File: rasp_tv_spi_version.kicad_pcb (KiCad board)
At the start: 2 copper layers, 118.3 x 53.5 mm, 12 parts, among them J1 Raspberry_Pi_2_3, J6 PAM8302-input, J7 PAM8302-output, J8 SPEAKER, J9 5V_USB, SW1 SW_Push_DPDT, U1 TFT_320x240

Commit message: make pcb routing
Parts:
- removed J9 (x2): 5V_USB, Connector_Wire:SolderWirePad_1x01_SMD_1.5x3mm
- removed U1: TFT_320x240, Display:TFT-320x240
- added J3: Conn_01x09, Connector_PinHeader_2.54mm:PinHeader_1x09_P2.54mm_Vertical_SMD_Pin1Left, F.Cu at (166.6, 91.1)
- added J4: AUODIO_IN, Connector_PinHeader_2.54mm:PinHeader_1x05_P2.54mm_Vertical_SMD_Pin1Left, F.Cu at (184.0, 77.5)
- added J5: SPEAKER, Connector_PinHeader_2.54mm:PinHeader_1x02_P2.54mm_Horizontal, B.Cu at (181.6, 87.6)
- added REF**: PinHeader_1x04_P2.54mm_Vertical, Connector_PinHeader_2.54mm:PinHeader_1x04_P2.54mm_Vertical, F.Cu at (85.6, 80.9)
- J1: footprint Connector_PinHeader_2.54mm:PinHeader_2x20_P2.54mm_Vertical -> Connector_PinSocket_2.54mm:PinSocket_2x20_P2.54mm_Vertical
- J6: value PAM8302-input -> AUDIO_OUT; footprint Connector_PinHeader_2.54mm:PinHeader_1x05_P2.54mm_Vertical -> Connector_PinSocket_2.54mm:PinSocket_1x02_P2.54mm_Vertical_SMD_Pin1Left; moved to F.Cu
- J7: value PAM8302-output -> AUDIO_OUT; footprint Connector_PinHeader_2.54mm:PinHeader_1x02_P2.54mm_Vertical -> Connector_PinSocket_2.54mm:PinSocket_1x02_P2.54mm_Vertical_SMD_Pin1Left; moved to F.Cu
- J8: value SPEAKER -> Conn_01x02_Pin; footprint Connector_Hirose:Hirose_DF13C_CL535-0402-2-51_1x02-1MP_P1.25mm_Vertical -> Connector_PinHeader_2.54mm:PinHeader_1x02_P2.54mm_Horizontal; moved to B.Cu
- SW1: footprint Button_Switch_THT:SW_Push_2P2T_Toggle_CK_PVA2OAH5xxxxxxV2 -> Button_Switch_THT:SW_DPDT_XLX
- moved J8 37.1 mm to (181.7, 103.5), turned to 0 degrees
- moved J6 33.8 mm to (186.9, 94.9), turned to -90 degrees
- moved J7 33.8 mm to (180.9, 94.9), turned to -90 degrees
- moved R2 30.9 mm to (145.4, 64.5)
- moved J1 30.0 mm to (91.5, 64.0)
- moved C1 29.0 mm to (145.3, 67.7)
- moved R1 28.4 mm to (145.3, 70.9)
- moved RV1 26.9 mm to (180.3, 63.5)
- moved SW1 21.8 mm to (187.9, 111.4), turned to 180 degrees
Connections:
- J1 pad 16: unconnected-(J1-GPIO23-Pad16) -> BACKLIGHT_23_GPIO
- J6 pad 1: Net-(J6-Pin_1) -> unconnected-(J6-Pin_1-Pad1)
- J6 pad 2: GND -> Net-(J5-Pin_1)
- J7 pad 1: Net-(J7-Pin_1) -> Net-(J5-Pin_2)
- J7 pad 2: Net-(J7-Pin_2) -> unconnected-(J7-Pin_2-Pad2)
- J8 pad 1: Net-(J7-Pin_1) -> Net-(J8-Pin_1)
- J8 pad 2: Net-(J7-Pin_2) -> Net-(J8-Pin_2)
- RV1 pad : GND -> (no net)
- RV1 pad 2: Net-(J6-Pin_1) -> AUDIO_IN
- SW1 pad 3: Net-(J9-Pin_2) -> Net-(J8-Pin_1)
- SW1 pad 4: unconnected-(SW1-A-Pad4) -> Net-(J8-Pin_2)
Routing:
- net +5V: track 31.5 -> 183.3 mm
- net BACKLIGHT_23_GPIO: track 0.00 -> 82.5 mm
- net +3.3V: track 38.2 -> 106.5 mm
- net CS_8_GPIO: track 46.2 -> 96.3 mm
- net GND: track 45.9 -> 0.00 mm
- net RESET_25_GPIO: track 48.3 -> 86.8 mm
- net DC_24_GPIO: track 46.6 -> 83.3 mm
- net Net-(J6-Pin_1): track 19.6 -> 0.00 mm
- net MOSI_0_10_GPIO: track 57.9 -> 77.3 mm
- net Net-(J7-Pin_2): track 18.6 -> 0.00 mm
- net AUDIO_IN: track 0.00 -> 16.6 mm
- net Net-(J7-Pin_1): track 14.7 -> 0.00 mm
- net Net-(J9-Pin_2): track 11.4 -> 0.00 mm
- net SCK_0_11_GPIO: track 57.8 -> 68.6 mm
- net Net-(J5-Pin_1): track 0.00 -> 10.6 mm
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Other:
- board size 118.3 x 53.5 mm -> 120 x 60 mm

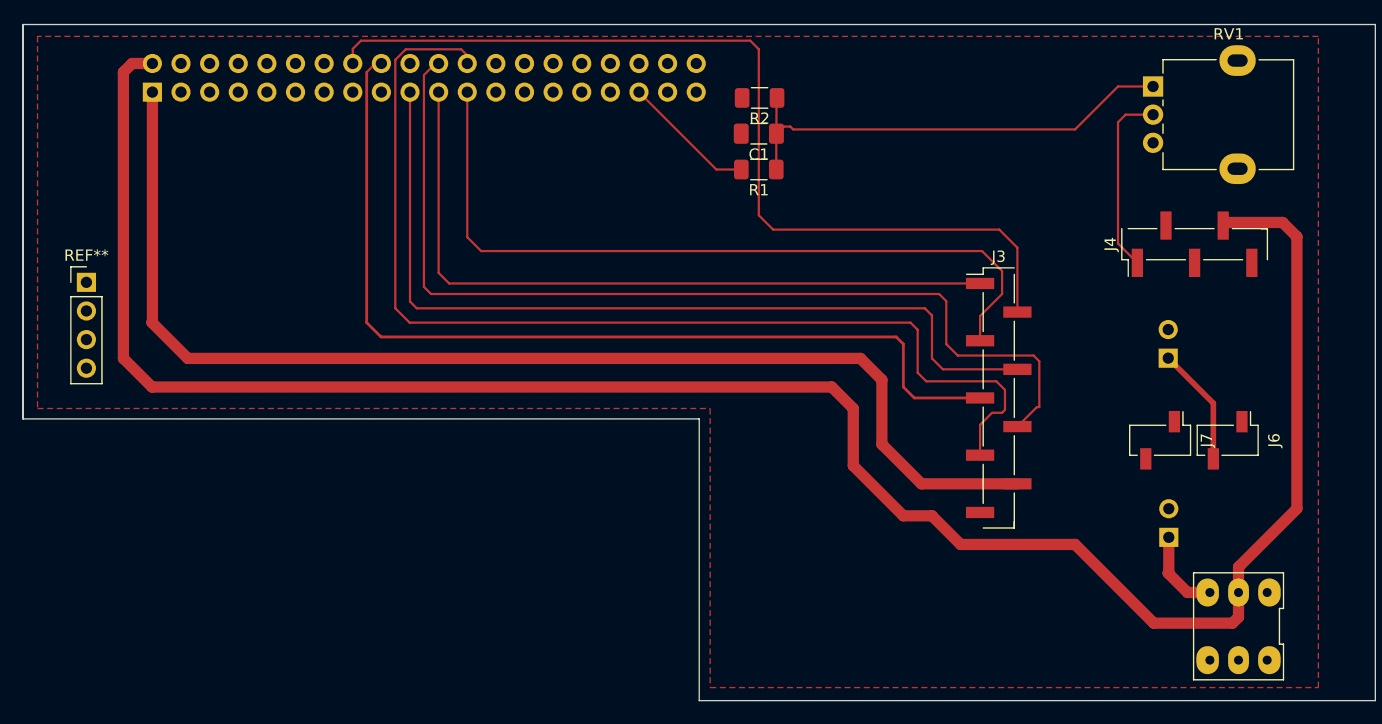
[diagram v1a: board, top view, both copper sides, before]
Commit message: finish board with 2.8 spi
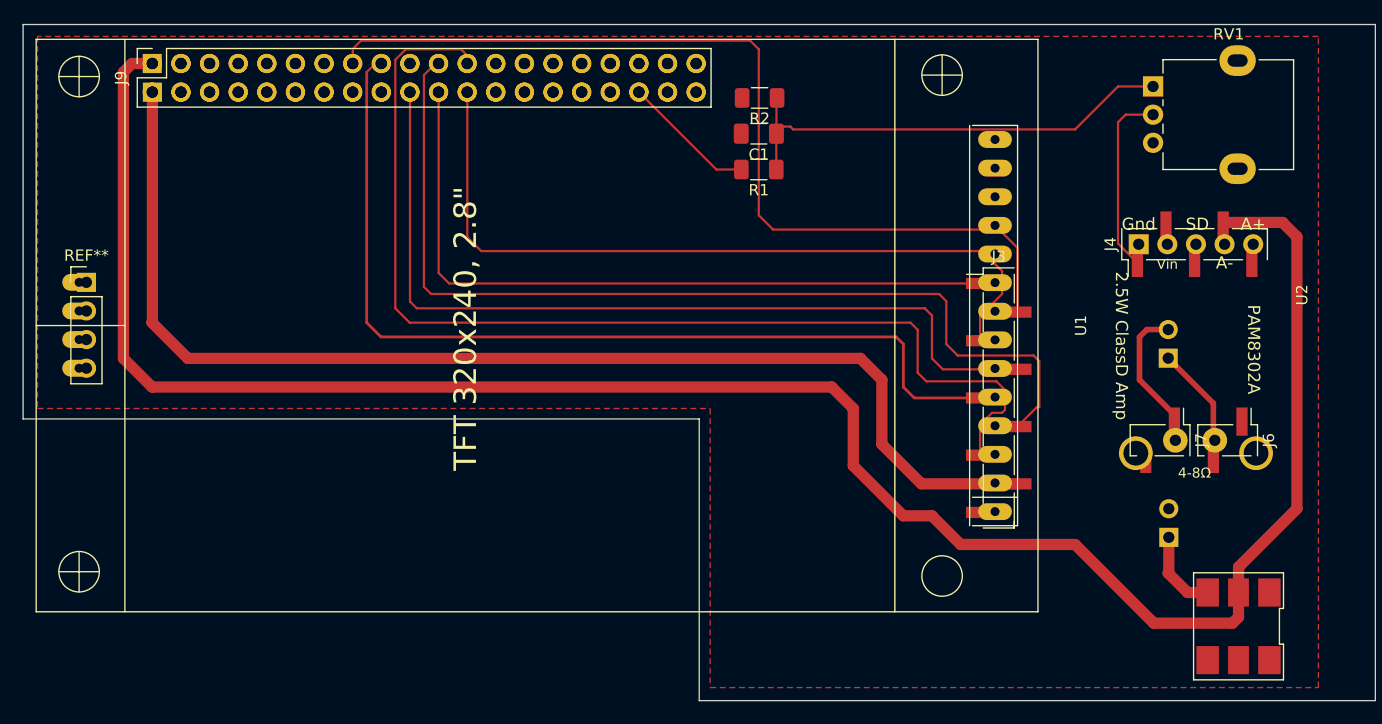
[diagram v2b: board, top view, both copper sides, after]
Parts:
- added J9: Raspberry_Pi_2_3, Connector_PinSocket_2.54mm:PinSocket_2x20_P2.54mm_Vertical, F.Cu at (91.5, 61.5)
- added U1: TFT_320x240, Display:TFT-320x240, F.Cu at (85.0, 106.6)
- added U2: PAM8302AAD, Module:PAM, F.Cu at (179.0, 77.5)
- J6, J7: footprint Connector_PinSocket_2.54mm:PinSocket_1x02_P2.54mm_Vertical_SMD_Pin1Left -> Connector_PinHeader_2.54mm:PinHeader_1x02_P2.54mm_Vertical_SMD_Pin1Left
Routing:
- net Net-(J5-Pin_2): track 0.00 -> 11.6 mm

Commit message: release 2.8
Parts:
- moved C1 62.2 mm to (91.0, 37.3)
- moved J3 62.2 mm to (112.3, 60.7)
- moved J4 62.2 mm to (129.7, 47.1)
- moved J5 62.2 mm to (127.4, 57.2)
- moved R1 62.2 mm to (91.0, 40.4)
- moved R2 62.2 mm to (91.1, 34.1)
- moved RV1 62.2 mm to (126.0, 33.1)
- moved U1 62.2 mm to (30.7, 76.1)
- moved U2 62.2 mm to (124.8, 47.1)
- moved J1 62.2 mm to (37.2, 33.6)
- moved J6 62.2 mm to (132.6, 64.5)
- moved J9 62.2 mm to (37.2, 31.0)
- moved REF** 62.2 mm to (31.4, 50.5)
- moved SW1 62.2 mm to (133.6, 81.0)
- moved J7 62.2 mm to (126.7, 64.5)
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
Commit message: ready for factory
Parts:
- removed the J4 at (129.7, 47.1)
- removed the J6 at (132.6, 64.5)
- removed the J7 at (126.7, 64.5)
- removed the J8 at (127.4, 73.1)
- removed REF**: PinHeader_1x04_P2.54mm_Vertical, Connector_PinHeader_2.54mm:PinHeader_1x04_P2.54mm_Vertical
- removed U2: PAM8302AAD, Module:PAM
- added 0.1u: C_Rect_L4.0mm_W2.5mm_P2.50mm, Capacitor_THT:C_Rect_L4.0mm_W2.5mm_P2.50mm, B.Cu at (247.6, 65.6)
- added 0.1u: C_Rect_L4.0mm_W2.5mm_P2.50mm, Capacitor_THT:C_Rect_L4.0mm_W2.5mm_P2.50mm, B.Cu at (224.6, 92.8)
- added 0.1u: C_Rect_L4.0mm_W2.5mm_P2.50mm, Capacitor_THT:C_Rect_L4.0mm_W2.5mm_P2.50mm, B.Cu at (249.5, 134.7)
- added 0.1u: C_Rect_L4.0mm_W2.5mm_P2.50mm, Capacitor_THT:C_Rect_L4.0mm_W2.5mm_P2.50mm, B.Cu at (97.5, 24.4)
- added 0.1u: C_Rect_L4.0mm_W2.5mm_P2.50mm, Capacitor_THT:C_Rect_L4.0mm_W2.5mm_P2.50mm, B.Cu at (122.4, 65.6)
- added 0.1u: C_Rect_L4.0mm_W2.5mm_P2.50mm, Capacitor_THT:C_Rect_L4.0mm_W2.5mm_P2.50mm, B.Cu at (222.6, 23.9)
- added 0.1uF: 0.1uF, Capacitor_SMD:C_1206_3216Metric_Pad1.33x1.80mm_HandSolder, F.Cu at (96.4, 26.3)
- added 0.1uF: 0.1uF, Capacitor_SMD:C_1206_3216Metric_Pad1.33x1.80mm_HandSolder, F.Cu at (125.2, 65.7)
- added 0.1uF: 0.1uF, Capacitor_SMD:C_1206_3216Metric_Pad1.33x1.80mm_HandSolder, F.Cu at (250.4, 65.7)
- added 0.1uF: 0.1uF, Capacitor_SMD:C_1206_3216Metric_Pad1.33x1.80mm_HandSolder, F.Cu at (252.3, 134.8)
- added 0R: R_1206_3216Metric, Resistor_SMD:R_1206_3216Metric, F.Cu at (186.5, 25.6)
- added 0R: R_1206_3216Metric, Resistor_SMD:R_1206_3216Metric, F.Cu at (188.5, 94.6)
- added 0R: R_1206_3216Metric, Resistor_SMD:R_1206_3216Metric, F.Cu at (237.0, 59.0)
- added 0R: R_1206_3216Metric, Resistor_SMD:R_1206_3216Metric, F.Cu at (239.3, 127.9)
- added 0R: , Resistor_SMD:R_1206_3216Metric, F.Cu at (61.5, 25.6)
- added 0R: , Resistor_SMD:R_1206_3216Metric, F.Cu at (111.6, 58.9)
- added 100R: R_Axial_DIN0204_L3.6mm_D1.6mm_P5.08mm_Horizontal, Resistor_THT:R_Axial_DIN0204_L3.6mm_D1.6mm_P5.08mm_Horizontal, B.Cu at (223.8, 30.9)
- added 100R: R_Axial_DIN0204_L3.6mm_D1.6mm_P5.08mm_Horizontal, Resistor_THT:R_Axial_DIN0204_L3.6mm_D1.6mm_P5.08mm_Horizontal, B.Cu at (225.8, 99.8)
- added 100R: R_Axial_DIN0204_L3.6mm_D1.6mm_P5.08mm_Horizontal, Resistor_THT:R_Axial_DIN0204_L3.6mm_D1.6mm_P5.08mm_Horizontal, B.Cu at (98.8, 31.0)
- added 100uF: CP_Radial_D5.0mm_P2.50mm, Capacitor_THT:CP_Radial_D5.0mm_P2.50mm, B.Cu at (249.9, 61.8)
- added 100uF: CP_Radial_D5.0mm_P2.50mm, Capacitor_THT:CP_Radial_D5.0mm_P2.50mm, B.Cu at (251.8, 130.9)
- added 100uF: CP_Radial_D5.0mm_P2.50mm, Capacitor_THT:CP_Radial_D5.0mm_P2.50mm, B.Cu at (124.7, 61.8)
- added 1K: 1K, Potentiometer_THT:Potentiometer_Alpha_RD901F-40-00D_Single_Vertical, F.Cu at (124.3, 22.1)
- added 220R: , Resistor_SMD:R_1206_3216Metric_Pad1.30x1.75mm_HandSolder, F.Cu at (96.2, 21.6)
- added 220R: 220R, Resistor_THT:R_Axial_DIN0204_L3.6mm_D1.6mm_P5.08mm_Horizontal, B.Cu at (98.8, 19.8)
- added 220R: 220R, Resistor_THT:R_Axial_DIN0204_L3.6mm_D1.6mm_P5.08mm_Horizontal, B.Cu at (225.8, 88.6)
- added 220R: 220R, Resistor_THT:R_Axial_DIN0204_L3.6mm_D1.6mm_P5.08mm_Horizontal, B.Cu at (223.8, 19.7)
- added ?: , , F.Cu at (251.8, 130.9)
- added ?: , , F.Cu at (247.6, 65.6)
- added ?: , , F.Cu at (252.3, 136.4)
- added ?: , , F.Cu at (247.6, 68.1)
- added ?: , , F.Cu at (224.6, 92.8)
- added C1: 0.1uF, Capacitor_SMD:C_1206_3216Metric_Pad1.33x1.80mm_HandSolder, F.Cu at (223.4, 95.3)
- added HOLD: PinHeader_1x02_P2.54mm_Vertical_SMD_Pin1Right, Connector_PinHeader_2.54mm:PinHeader_1x02_P2.54mm_Vertical_SMD_Pin1Right, F.Cu at (160.4, 109.8)
- added HOLD: HOLD, Connector_PinHeader_2.54mm:PinHeader_1x02_P2.54mm_Vertical_SMD_Pin1Right, F.Cu at (161.7, 40.8)
- added HOLD: PinHeader_1x02_P2.54mm_Vertical_SMD_Pin1Right, Connector_PinHeader_2.54mm:PinHeader_1x02_P2.54mm_Vertical_SMD_Pin1Right, F.Cu at (22.9, 40.8)
- added J3: Conn_01x09, Connector_PinHeader_2.54mm:PinHeader_1x09_P2.54mm_Vertical_SMD_Pin1Left, F.Cu at (117.7, 49.7)
- added J4: Conn_01x05_Pin, Connector_PinHeader_2.54mm:PinHeader_1x05_P2.54mm_Vertical, B.Cu at (249.7, 34.7)
- added J4: Conn_01x05_Pin, Connector_PinHeader_2.54mm:PinHeader_1x05_P2.54mm_Vertical, B.Cu at (124.7, 34.7)
- added J6: OUT1, Connector_PinHeader_2.54mm:PinHeader_1x01_P2.54mm_Vertical, B.Cu at (128.1, 52.1)
- added J6: OUT1, Connector_PinHeader_2.54mm:PinHeader_1x01_P2.54mm_Vertical, B.Cu at (255.1, 121.1)
- added J6: OUT1, Connector_PinHeader_2.54mm:PinHeader_1x01_P2.54mm_Vertical, B.Cu at (253.1, 52.1)
- added J7: OUT2, Connector_PinHeader_2.54mm:PinHeader_1x01_P2.54mm_Vertical, B.Cu at (131.6, 52.1)
- added J7: OUT2, Connector_PinHeader_2.54mm:PinHeader_1x01_P2.54mm_Vertical, B.Cu at (256.6, 52.1)
- added J7: OUT2, Connector_PinHeader_2.54mm:PinHeader_1x01_P2.54mm_Vertical, B.Cu at (258.6, 121.1)
- added J8: Conn_01x02_Pin, Connector_Wire:SolderWire-0.1sqmm_1x02_P3.6mm_D0.4mm_OD1mm, F.Cu at (260.9, 57.0)
- added J8: Conn_01x02_Pin, Connector_Wire:SolderWire-0.1sqmm_1x02_P3.6mm_D0.4mm_OD1mm, F.Cu at (262.9, 126.0)
- added J8: Conn_01x02_Pin, Connector_Wire:SolderWire-0.1sqmm_1x02_P3.6mm_D0.4mm_OD1mm, F.Cu at (135.9, 57.0)
- added J9: Raspberry_Pi_2_3, Connector_PinSocket_2.54mm:PinSocket_2x20_P2.54mm_Vertical, F.Cu at (42.6, 20.0)
- added J9: Raspberry_Pi_2_3, Connector_PinSocket_2.54mm:PinSocket_2x20_P2.54mm_Vertical, F.Cu at (169.6, 89.0)
- added PAM8302: PAM, Module:PAM, B.Cu at (259.9, 34.7)
- added PAM8302: PAM, Module:PAM, B.Cu at (262.0, 103.7)
- added PAM8302: PAM, Module:PAM, B.Cu at (134.9, 34.7)
- added PAM8302: Conn_01x05_Pin, Connector_PinHeader_2.54mm:PinHeader_1x05_P2.54mm_Vertical, B.Cu at (251.7, 103.7)
- added R1: 100E, Resistor_SMD:R_1206_3216Metric_Pad1.30x1.75mm_HandSolder, F.Cu at (223.4, 98.4)
- added R1: 100R, Resistor_SMD:R_1206_3216Metric_Pad1.30x1.75mm_HandSolder, F.Cu at (96.4, 29.4)
- added R2: 220E, Resistor_SMD:R_1206_3216Metric_Pad1.30x1.75mm_HandSolder, F.Cu at (223.4, 90.6)
- added RV1: 1K, Potentiometer_THT:Potentiometer_Alpha_RD901F-40-00D_Single_Vertical, F.Cu at (251.3, 91.1)
- added Raspberry_Pi_ZERO: Raspberry_Pi_2_3, Connector_PinSocket_2.54mm:PinSocket_2x20_P2.54mm_Vertical, B.Cu at (42.6, 22.6)
- added Raspberry_Pi_ZERO: Raspberry_Pi_2_3, Connector_PinSocket_2.54mm:PinSocket_2x20_P2.54mm_Vertical, B.Cu at (169.6, 91.6)
- added SPEAKER: SPEAKER, Connector_Hirose:Hirose_DF3EA-02P-2V_1x02-1MP_P2.00mm_Vertical, F.Cu at (253.2, 43.3)
- added SPEAKER: SPEAKER, Connector_Hirose:Hirose_DF3EA-02P-2V_1x02-1MP_P2.00mm_Vertical, F.Cu at (128.2, 43.3)
- added SW: SW_Push_DPDT, Button_Switch_THT:SW_DPDT_XLX, F.Cu at (131.8, 64.0)
- added SW: SW_Push_DPDT, Button_Switch_THT:SW_DPDT_XLX, F.Cu at (258.8, 133.0)
- added TFT320x240,3.2": Conn_01x09, Connector_PinHeader_2.54mm:PinHeader_1x09_P2.54mm_Vertical_SMD_Pin1Left, F.Cu at (244.7, 118.7)
- added U1: TFT_320x240, Display:TFT-320x240, F.Cu at (163.3, 134.3)
- added U1: TFT_320x240, Display:TFT-320x240, F.Cu at (35.9, 65.3)
- J5: footprint Connector_PinHeader_2.54mm:PinHeader_1x02_P2.54mm_Horizontal -> Connector_Hirose:Hirose_DF3EA-02P-2V_1x02-1MP_P2.00mm_Vertical; moved to F.Cu
- Raspberry_Pi_ZERO: renamed from J1; value Raspberry_Pi_2_3 -> Raspberry_Pi_ZERO
- SW: renamed from SW1; value SW_Push_DPDT -> SW
- moved J5 139.2 mm to (255.2, 112.3), turned to 90 degrees
- moved R2 130.9 mm to (221.4, 21.7)
- moved J9 130.9 mm to (167.6, 20.0)
- moved R1 130.8 mm to (221.4, 29.4)
- moved TFT320x240,2.8" 130.8 mm to (242.7, 49.7)
- moved C1 130.8 mm to (221.4, 26.3)
- moved Raspberry_Pi_ZERO 130.8 mm to (167.6, 22.6)
- moved U1 130.7 mm to (160.9, 65.3)
- moved SW 124.4 mm to (256.8, 64.0), turned to 0 degrees
- moved 1K 123.8 mm to (249.3, 22.1)
- renumbered RV1 to 1K, J3 to TFT320x240,2.8"
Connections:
- 1K pad : (no net) -> GND
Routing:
- net +5V: track 183.3 -> 511.5 mm
- net BACKLIGHT_23_GPIO: track 82.5 -> 255.0 mm
- net CS_8_GPIO: track 96.3 -> 268.0 mm
- net RESET_25_GPIO: track 86.8 -> 257.6 mm
- net DC_24_GPIO: track 83.3 -> 227.6 mm
- net +3.3V: track 106.5 -> 249.3 mm
- net MOSI_0_10_GPIO: track 77.3 -> 211.9 mm
- net SCK_0_11_GPIO: track 68.6 -> 196.7 mm
- net MISO_0_09_GPIO: track 64.5 -> 173.1 mm
- net Net-(C1-Pad1): track 42.2 -> 121.3 mm
- net Net-(J5-Pin_2): track 11.6 -> 58.3 mm
- net Net-(J8-Pin_2): track 0.01 -> 32.6 mm
- net Net-(J8-Pin_1): track 7.62 -> 38.4 mm
- net PWM_19_GPIO: track 11.9 -> 41.5 mm
- net AUDIO_IN: track 16.6 -> 39.7 mm
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- added copper zone on F.Cu, net +5V
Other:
- board size 120 x 60 mm -> 247 x 123 mm
- board text added: "+"
- board text added: "-"
- board text added: "PAM8302A"
